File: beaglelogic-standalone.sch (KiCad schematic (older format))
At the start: 247 parts, among them J1 USB_OTG, J2 CONN_02X02, J3 USB_A, J4 CONN_01X06, J5 SI-51009-F, J6 CONN_02X12, J7 CONN_02X16, Q1 BSS138, Q2 BSS138, SW1 SW_PUSH_SMALL_H, SW2 SW_PUSH_SMALL_H, U1 74LVC1G07, U10 MCP79410/TDFN, U11 SST26VF064B, U12 TPS73101, U13 SN74LVCH16T245, U14 DVIULC6-4SC6, U15 DVIULC6-4SC6, U16 DVIULC6-4SC6, U17 DVIULC6-4SC6, U18 74LV1T125, U19 EMMC_4G, U2 AP1117, U3 TPS2051C, U4 TPD4S012, U5 TPD4S012, U6 OSD3358-SM, U7 KSZ9031RNXCC, U8 74LVC2G241, U9 74LVC1G125, Y1 25MHz, Y2 24MHz, Y3 32.768kHz,CL=9pF

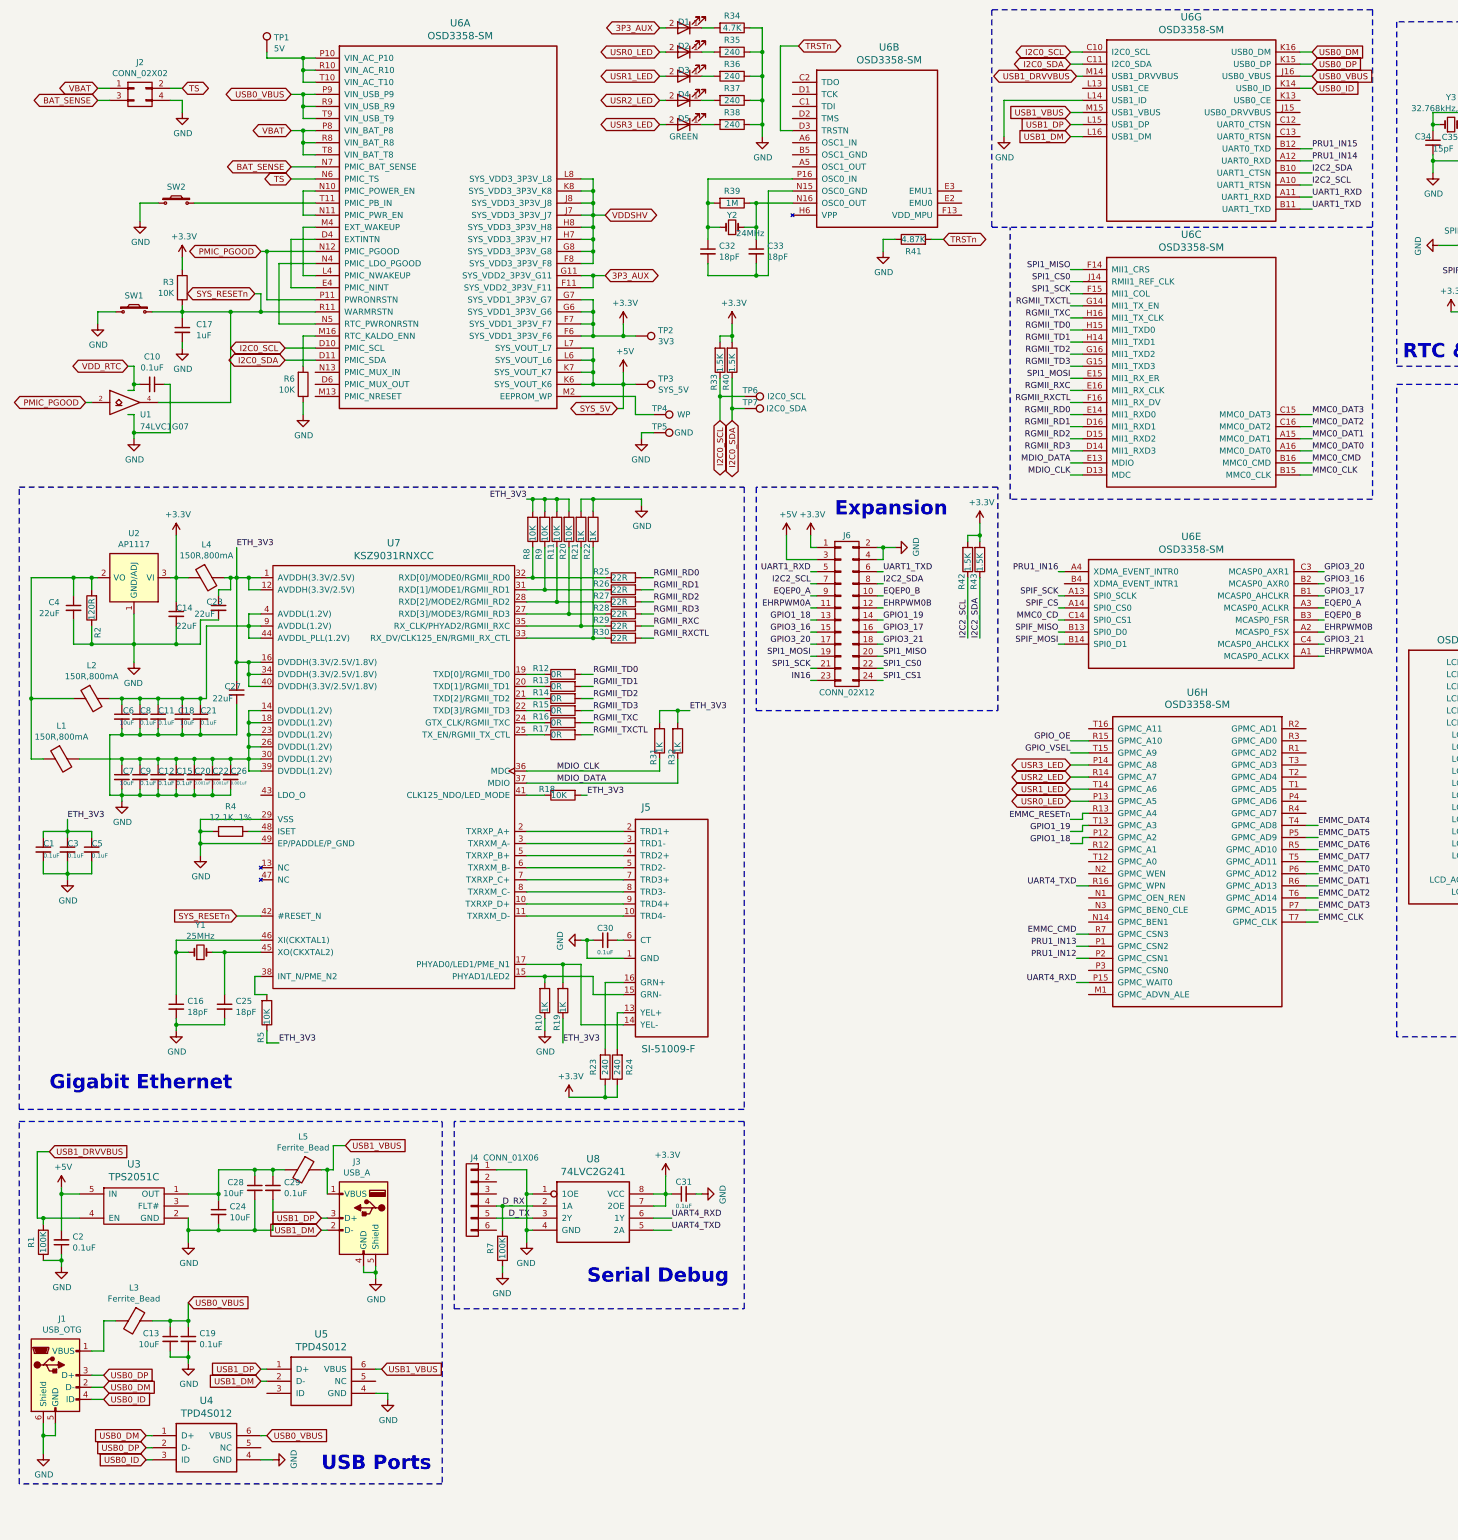
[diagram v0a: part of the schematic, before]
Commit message: PCB layout: Initial commit
First pass at component placement.
Also, slight changes in schematic.

Signed-off-by: Kumar Abhishek <abhishek@theembeddedkitchen.net>
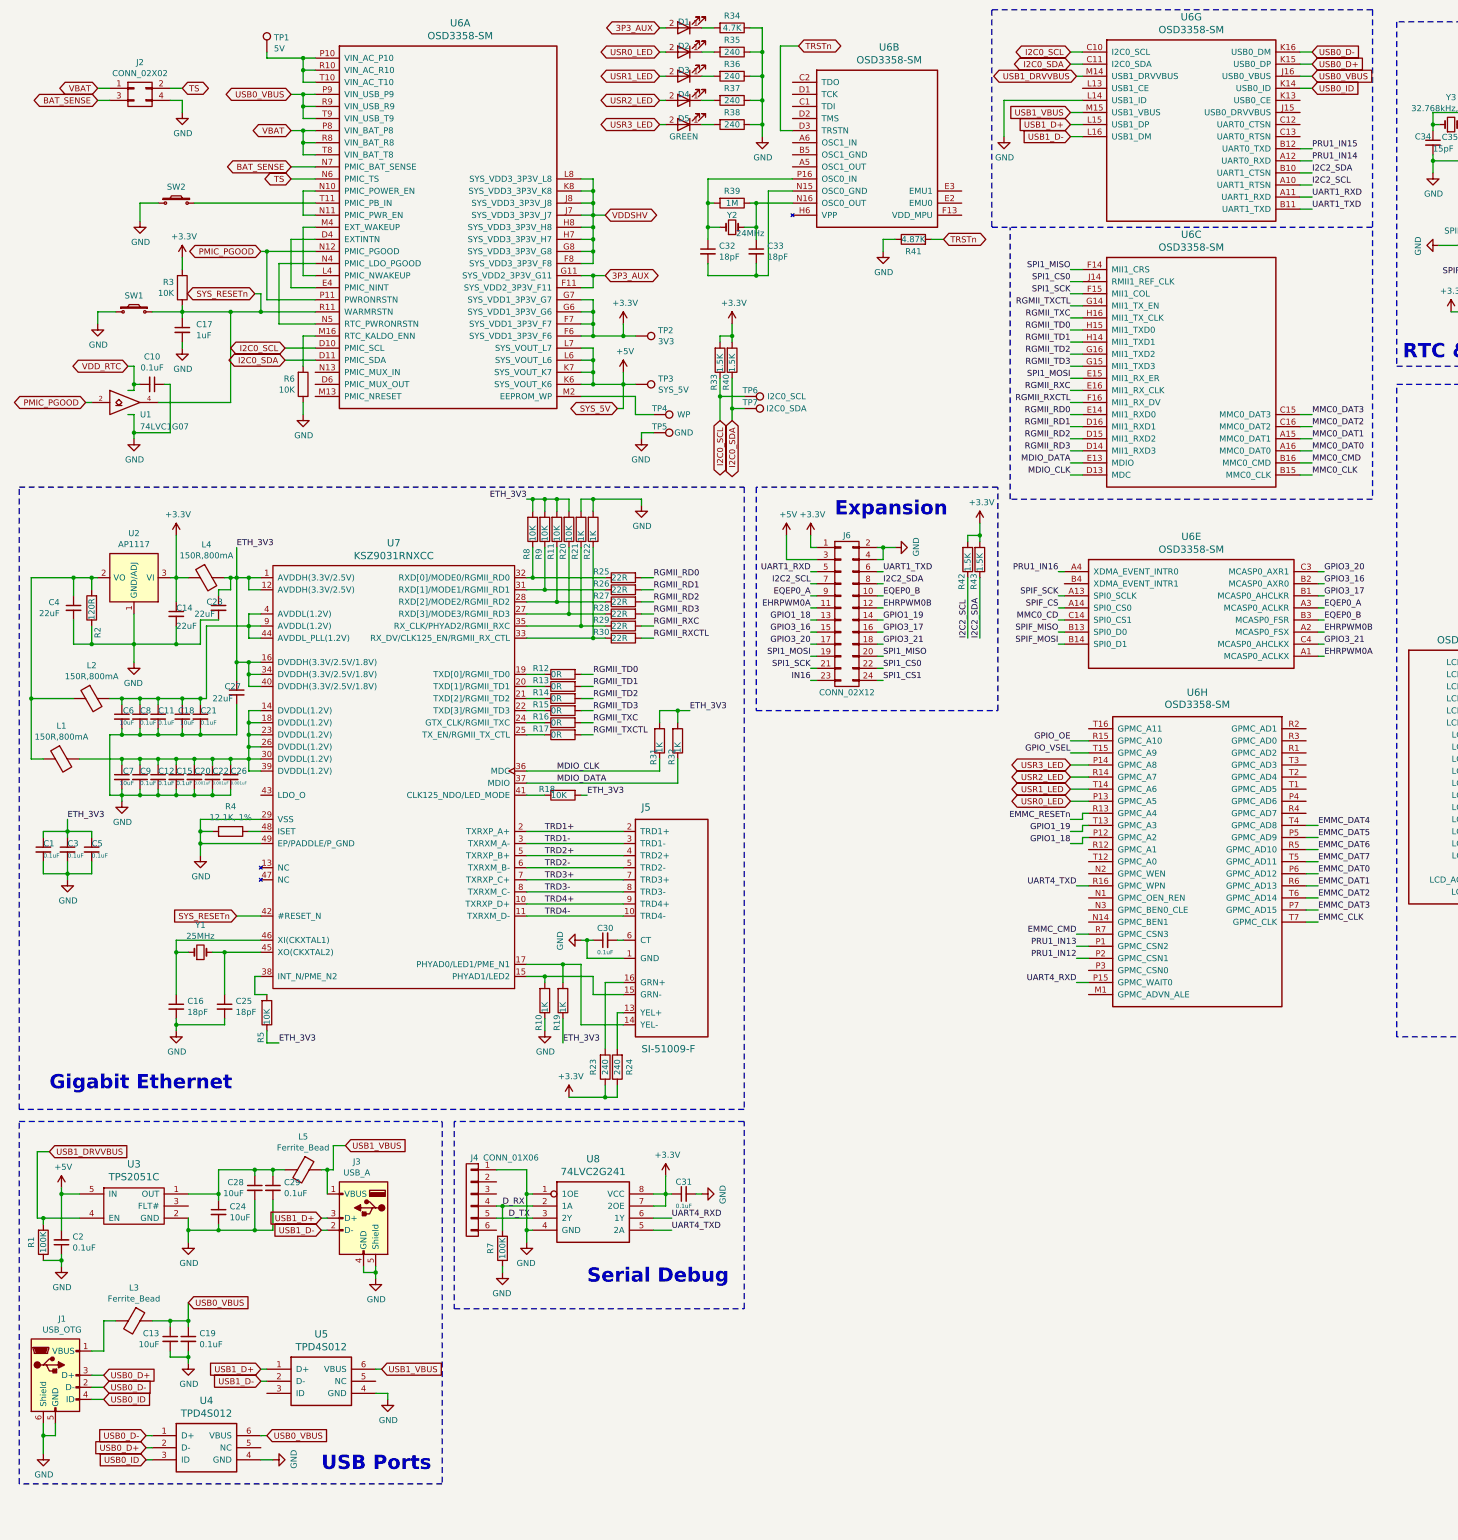
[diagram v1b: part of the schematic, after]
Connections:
- net TRD4-: now reaches J5.10 (TRD4-), U7.11 (TXRXM_D-)
- net TRD1+: now reaches J5.2 (TRD1+), U7.2 (TXRXP_A+)
- net TRD1-: now reaches J5.3 (TRD1-), U7.3 (TXRXM_A-)
- net TRD2+: now reaches J5.4 (TRD2+), U7.5 (TXRXP_B+)
- net TRD2-: now reaches J5.5 (TRD2-), U7.6 (TXRXM_B-)
- net TRD3+: now reaches J5.7 (TRD3+), U7.7 (TXRXP_C+)
- net TRD3-: now reaches J5.8 (TRD3-), U7.8 (TXRXM_C-)
- net TRD4+: now reaches J5.9 (TRD4+), U7.10 (TXRXP_D+)
- net USB0_DM renamed USB0_D-
- net USB0_DP renamed USB0_D+
- net USB1_DM renamed USB1_D-
- net USB1_DP renamed USB1_D+
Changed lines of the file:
@@
 MMC0_CD
 Text GLabel 1200 11900 2    50   Input ~ 0
-USB0_DM
+USB0_D-
 Text GLabel 1200 11800 2    50   Input ~ 0
-USB0_DP
+USB0_D+
 $Comp
 L Ferrite_Bead L3
@@
 $EndComp
 Text GLabel 3000 10500 0    50   Input ~ 0
-USB1_DP
+USB1_D+
 Text GLabel 3000 10600 0    50   Input ~ 0
-USB1_DM
+USB1_D-
 Text GLabel 3200 9900 2    50   Input ~ 0
 USB1_VBUS
@@
 USB1_VBUS
 Text GLabel 9200 1450 0    50   Input ~ 0
-USB1_DP
+USB1_D+
 Text GLabel 9200 1550 0    50   Input ~ 0
-USB1_DM
+USB1_D-
 $Comp
 L GND #PWR051
@@
 $EndComp
 Text GLabel 11200 850  2    50   Input ~ 0
-USB0_DM
+USB0_D-
 Text GLabel 11200 950  2    50   Input ~ 0
-USB0_DP
+USB0_D+
 Text GLabel 11200 1150 2    50   Input ~ 0
 USB0_ID
@@
 $EndComp
 Text GLabel 1550 12400 0    50   Input ~ 0
-USB0_DP
+USB0_D+
 Text GLabel 1550 12300 0    50   Input ~ 0
-USB0_DM
+USB0_D-
 Text GLabel 1550 12500 0    50   Input ~ 0
 USB0_ID
@@
 $EndComp
 Text GLabel 2500 11750 0    50   Input ~ 0
-USB1_DP
+USB1_D+
 Text GLabel 2500 11850 0    50   Input ~ 0
-USB1_DM
+USB1_D-
 $Comp
 L GND #PWR086
@@
 Connection ~ 17200 7400
 Connection ~ 18700 7400
+Text Label 4850 7300 0    50   ~ 0
+TRD1+
+Text Label 4850 7400 0    50   ~ 0
+TRD1-
+Text Label 4850 7500 0    50   ~ 0
+TRD2+
+Text Label 4850 7600 0    50   ~ 0
+TRD2-
+Text Label 4850 7700 0    50   ~ 0
+TRD3+
+Text Label 4850 7800 0    50   ~ 0
+TRD3-
+Text Label 4850 7900 0    50   ~ 0
+TRD4+
+Text Label 4850 8000 0    50   ~ 0
+TRD4-
 $EndSCHEMATC

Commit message: Update routing and schematic
Signed-off-by: Kumar Abhishek <abhishek@theembeddedkitchen.net>
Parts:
- removed TP1: 5V, Measurement_Points:Measurement_Point_Round-SMD-Pad_Small, symbol TEST_1P
- added J8: Barrel_Jack, Connect:BARREL_JACK, symbol Barrel_Jack
- added LOGO1: TEST_1P, beaglelogic-standalone:beaglelogic-logo, symbol Mounting_Hole
- added M1, M2, M3, M4: TEST_1P, Mounting_Holes:MountingHole_3.2mm_M3, symbol Mounting_Hole
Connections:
- net DIN00: now also U13.2 (1B1); no longer U13.23 (2B8)
- net DIN01: now also U13.3 (1B2); no longer U13.22 (2B7)
- net DIN02: now also U13.5 (1B3); no longer U13.20 (2B6)
- net DIN03: now also U13.6 (1B4); no longer U13.19 (2B5)
- net DIN04: now also U13.8 (1B5); no longer U13.17 (2B4)
- net DIN05: now also U13.9 (1B6); no longer U13.16 (2B3)
- net DIN06: now also U13.11 (1B7); no longer U13.14 (2B2)
- net DIN07: now also U13.12 (1B8); no longer U13.13 (2B1)
- net DIN08: now also U13.13 (2B1); no longer U13.12 (1B8)
- net DIN09: now also U13.14 (2B2); no longer U13.11 (1B7)
- net DIN10: now also U13.16 (2B3); no longer U13.9 (1B6)
- net DIN11: now also U13.17 (2B4); no longer U13.8 (1B5)
- net DIN12: now also U13.19 (2B5); no longer U13.6 (1B4)
- net DIN13: now also U13.20 (2B6); no longer U13.5 (1B3)
- net DIN14: now also U13.22 (2B7); no longer U13.3 (1B2)
- net DIN15: now also U13.23 (2B8); no longer U13.2 (1B1)
- net GND: now also J8.2
- net I2C2_SCL: now also J6.8 (P8); no longer J6.7 (P7)
- net I2C2_SDA: now also J6.7 (P7); no longer J6.8 (P8)
- net PRU1_IN00: now also U13.47 (1A1); no longer U13.26 (2A8)
- net PRU1_IN01: now also U13.46 (1A2); no longer U13.27 (2A7)
- net PRU1_IN02: now also U13.44 (1A3); no longer U13.29 (2A6)
- net PRU1_IN03: now also RN1.8 (R1.2), U13.43 (1A4); no longer RN1.5 (R4.2), U13.30 (2A5)
- net PRU1_IN04: now also RN1.7 (R2.2), U13.41 (1A5); no longer RN1.6 (R3.2), U13.32 (2A4)
- net PRU1_IN05: now also RN1.6 (R3.2), U13.40 (1A6); no longer RN1.7 (R2.2), U13.33 (2A3)
- net PRU1_IN06: now also U13.38 (1A7); no longer U13.35 (2A2)
- net PRU1_IN07: now also U13.37 (1A8); no longer U13.36 (2A1)
- net PRU1_IN08: now also U13.36 (2A1); no longer U13.37 (1A8)
- net PRU1_IN09: now also U13.35 (2A2); no longer U13.38 (1A7)
- net PRU1_IN10: now also U13.33 (2A3); no longer U13.40 (1A6)
- net PRU1_IN11: now also U13.32 (2A4); no longer U13.41 (1A5)
- net PRU1_IN12: now also U13.30 (2A5); no longer U13.43 (1A4)
- net PRU1_IN13: now also U13.29 (2A6); no longer U13.44 (1A3)
- net PRU1_IN14: now also U13.27 (2A7); no longer U13.46 (1A2)
- net PRU1_IN15: now also U13.26 (2A8); no longer U13.47 (1A1)
- net UART1_RXD: now also J6.6 (P6); no longer J6.5 (P5)
- net UART1_TXD: now also J6.5 (P5); no longer J6.6 (P6)
- net 5V_IN: now reaches U6.P10 (VIN_AC_P10), U6.R10 (VIN_AC_R10), U6.T10 (VIN_AC_T10)
- net 5V_IN: now also J8.1
- net at U6.L1 (LCD_DATA14): now also RN1.5 (R4.2); no longer RN1.8 (R1.2)
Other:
- note added: "Mounting holes\n"
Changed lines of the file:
@@
 LIBS:contrib
 LIBS:valves
+LIBS:mechanical
+LIBS:graphic_symbols
 LIBS:beaglelogic-standalone-cache
 EELAYER 26 0
@@
 L R_Pack04 RN1
 U 1 1 5961EA54
-P 13400 5550
-F 0 "RN1" H 13120 5504 50  0000 R CNN
-F 1 "100K" H 13120 5595 50  0000 R CNN
-F 2 "Resistors_SMD:R_Array_Concave_4x0402" V 13675 5550 50  0001 C CNN
-F 3 "" H 13400 5550 50  0001 C CNN
-	1    13400 5550
-	-1   0    0    1
+P 13500 5550
+F 0 "RN1" H 13220 5504 50  0000 R CNN
+F 1 "100K" H 13220 5595 50  0000 R CNN
+F 2 "Resistors_SMD:R_Array_Concave_4x0402" V 13775 5550 50  0001 C CNN
+F 3 "" H 13500 5550 50  0001 C CNN
+	1    13500 5550
+	1    0    0    1
 $EndComp
 $Comp
@@
 	1    0    0    -1
 $EndComp
-Text Label 17300 7900 0    50   ~ 0
+Text Label 17300 5800 0    50   ~ 0
 DIN00
-Text Label 17300 7800 0    50   ~ 0
+Text Label 17300 5900 0    50   ~ 0
 DIN01
 Text Label 21950 5650 2    50   ~ 0
@@
 Text Label 20200 5500 0    50   ~ 0
 IN02
-Text Label 17300 7600 0    50   ~ 0
+Text Label 17300 6100 0    50   ~ 0
 DIN02
-Text Label 17300 7500 0    50   ~ 0
+Text Label 17300 6200 0    50   ~ 0
 DIN03
-Text Label 17300 7300 0    50   ~ 0
+Text Label 17300 6400 0    50   ~ 0
 DIN04
-Text Label 17300 7200 0    50   ~ 0
+Text Label 17300 6500 0    50   ~ 0
 DIN05
-Text Label 17300 7000 0    50   ~ 0
+Text Label 17300 6700 0    50   ~ 0
 DIN06
-Text Label 17300 6900 0    50   ~ 0
-DIN07
 Text Label 17300 6800 0    50   ~ 0
+DIN07
+Text Label 17300 6900 0    50   ~ 0
 DIN08
-Text Label 17300 6700 0    50   ~ 0
+Text Label 17300 7000 0    50   ~ 0
 DIN09
-Text Label 17300 6500 0    50   ~ 0
+Text Label 17300 7200 0    50   ~ 0
 DIN10
-Text Label 17300 6400 0    50   ~ 0
+Text Label 17300 7300 0    50   ~ 0
 DIN11
-Text Label 17300 6200 0    50   ~ 0
+Text Label 17300 7500 0    50   ~ 0
 DIN12
-Text Label 17300 6100 0    50   ~ 0
+Text Label 17300 7600 0    50   ~ 0
 DIN13
-Text Label 17300 5900 0    50   ~ 0
+Text Label 17300 7800 0    50   ~ 0
 DIN14
-Text Label 17300 5800 0    50   ~ 0
+Text Label 17300 7900 0    50   ~ 0
 DIN15
 Text Label 19350 4950 2    50   ~ 0
@@
 	1    0    0    -1
 $EndComp
-Text Label 15200 7900 2    50   ~ 0
+Text Label 15200 5800 2    50   ~ 0
 PRU1_IN00
-Text Label 15200 7800 2    50   ~ 0
+Text Label 15200 5900 2    50   ~ 0
 PRU1_IN01
-Text Label 15200 7600 2    50   ~ 0
+Text Label 15200 6100 2    50   ~ 0
 PRU1_IN02
-Text Label 15200 7500 2    50   ~ 0
+Text Label 15200 6200 2    50   ~ 0
 PRU1_IN03
-Text Label 15200 7300 2    50   ~ 0
+Text Label 15200 6400 2    50   ~ 0
 PRU1_IN04
-Text Label 15200 7200 2    50   ~ 0
+Text Label 15200 6500 2    50   ~ 0
 PRU1_IN05
-Text Label 15200 7000 2    50   ~ 0
+Text Label 15200 6700 2    50   ~ 0
 PRU1_IN06
-Text Label 15200 6900 2    50   ~ 0
-PRU1_IN07
 Text Label 15200 6800 2    50   ~ 0
+PRU1_IN07
+Text Label 15200 6900 2    50   ~ 0
 PRU1_IN08
-Text Label 15200 6700 2    50   ~ 0
+Text Label 15200 7000 2    50   ~ 0
 PRU1_IN09
-Text Label 15200 6500 2    50   ~ 0
+Text Label 15200 7200 2    50   ~ 0
 PRU1_IN10
-Text Label 15200 6400 2    50   ~ 0
+Text Label 15200 7300 2    50   ~ 0
 PRU1_IN11
-Text Label 15200 6200 2    50   ~ 0
+Text Label 15200 7500 2    50   ~ 0
 PRU1_IN12
-Text Label 15200 6100 2    50   ~ 0
+Text Label 15200 7600 2    50   ~ 0
 PRU1_IN13
-Text Label 15200 5900 2    50   ~ 0
+Text Label 15200 7800 2    50   ~ 0
 PRU1_IN14
-Text Label 15200 5800 2    50   ~ 0
+Text Label 15200 7900 2    50   ~ 0
 PRU1_IN15
 $Comp
@@
 	1    0    0    -1
 $EndComp
-$Comp
-L TEST_1P TP1
-U 1 1 5976DB01
-P 2550 850
-F 0 "TP1" H 2608 970 50  0000 L CNN
-F 1 "5V" H 2608 879 50  0000 L CNN
-F 2 "Measurement_Points:Measurement_Point_Round-SMD-Pad_Small" H 2750 850 50  0001 C CNN
-F 3 "" H 2750 850 50  0001 C CNN
-	1    2550 850
-	1    0    0    -1
-$EndComp
 Text GLabel 1400 3450 0    50   BiDi ~ 0
 VDD_RTC
@@
 	-1   0    0    -1
 $EndComp
-Text Label 7050 5150 2    50   ~ 0
+Text Label 7650 5150 0    50   ~ 0
 UART1_RXD
 Text Label 11200 2050 0    50   ~ 0
@@
 Text Label 9250 7750 2    50   ~ 0
 UART4_TXD
-Text Label 7650 5150 0    50   ~ 0
+Text Label 7050 5150 2    50   ~ 0
 UART1_TXD
-Text Label 7650 5250 0    50   ~ 0
-I2C2_SDA
 Text Label 7050 5250 2    50   ~ 0
+I2C2_SDA
+Text Label 7650 5250 0    50   ~ 0
 I2C2_SCL
 Text Label 7050 5350 2    50   ~ 0
@@
 	2850 900  2850 1100
 Wire Wire Line
-	2550 900  2950 900
+	2750 900  2950 900
 Wire Wire Line
 	2950 1300 2850 1300
@@
 Wire Wire Line
 	1500 2100 1500 2250
-Wire Wire Line
-	2550 850  2550 900
 Connection ~ 2850 900
 Wire Wire Line
@@
 Wire Wire Line
 	16900 7400 18700 7400
-Connection ~ 17200 7400
-Connection ~ 18700 7400
 Text Label 4850 7300 0    50   ~ 0
 TRD1+
@@
 Text Label 4850 8000 0    50   ~ 0
 TRD4-
+Connection ~ 18700 7400
+Connection ~ 17200 7400
+$Comp
+L Mounting_Hole M1
+U 1 1 59A18719
+P 4550 11750
+F 0 "M1" H 4550 11895 50  0000 C CNN
+F 1 "TEST_1P" H 4608 11779 50  0001 L CNN
+F 2 "Mounting_Holes:MountingHole_3.2mm_M3" H 4750 11750 50  0001 C CNN
+F 3 "" H 4750 11750 50  0001 C CNN
+	1    4550 11750
+	1    0    0    -1
+$EndComp
+$Comp
+L Mounting_Hole M2
+U 1 1 59A1A3C5
+P 4750 11750
+F 0 "M2" H 4750 11895 50  0000 C CNN
+F 1 "TEST_1P" H 4808 11779 50  0001 L CNN
+F 2 "Mounting_Holes:MountingHole_3.2mm_M3" H 4950 11750 50  0001 C CNN
+F 3 "" H 4950 11750 50  0001 C CNN
+	1    4750 11750
+	1    0    0    -1
+$EndComp
+$Comp
+L Mounting_Hole M3
+U 1 1 59A1A5E5
+P 4950 11750
+F 0 "M3" H 4950 11895 50  0000 C CNN
+F 1 "TEST_1P" H 5008 11779 50  0001 L CNN
+F 2 "Mounting_Holes:MountingHole_3.2mm_M3" H 5150 11750 50  0001 C CNN
+F 3 "" H 5150 11750 50  0001 C CNN
+	1    4950 11750
+	1    0    0    -1
+$EndComp
+Wire Notes Line
+	4100 11300 4100 12700
+Wire Notes Line
+	4100 12700 6500 12700
+Wire Notes Line
+	6500 12700 6500 11300
+Wire Notes Line
+	6500 11300 4100 11300
+Text Notes 4950 12600 0    118  ~ 24
+Mounting holes\n
+$Comp
+L Mounting_Hole LOGO1
+U 1 1 59A1CFE2
+P 5500 11750
+F 0 "LOGO1" H 5600 11750 50  0000 L CNN
+F 1 "TEST_1P" H 5558 11779 50  0001 L CNN
+F 2 "beaglelogic-standalone:beaglelogic-logo" H 5700 11750 50  0001 C CNN
+F 3 "" H 5700 11750 50  0001 C CNN
+	1    5500 11750
+	1    0    0    -1
+$EndComp
+$Comp
+L Barrel_Jack J8
+U 1 1 59A1E8AF
+P 950 1700
+F 0 "J8" H 1028 2025 50  0000 C CNN
+F 1 "Barrel_Jack" H 1028 1934 50  0000 C CNN
+F 2 "Connect:BARREL_JACK" H 1000 1660 50  0001 C CNN
+F 3 "" H 1000 1660 50  0001 C CNN
+	1    950  1700
+	1    0    0    -1
+$EndComp
+$Comp
+L GND #PWR097
+U 1 1 59A224A3
+P 1350 1850
+F 0 "#PWR097" H 1350 1600 50  0001 C CNN
+F 1 "GND" H 1355 1677 50  0000 C CNN
+F 2 "" H 1350 1850 50  0001 C CNN
+F 3 "" H 1350 1850 50  0001 C CNN
+	1    1350 1850
+	1    0    0    -1
+$EndComp
+Wire Wire Line
+	1250 1800 1350 1800
+Wire Wire Line
+	1350 1800 1350 1850
+Text GLabel 2750 900  0    50   BiDi ~ 0
+5V_IN
+Text GLabel 1350 1600 2    50   BiDi ~ 0
+5V_IN
+Wire Wire Line
+	1350 1600 1250 1600
+$Comp
+L Mounting_Hole M4
+U 1 1 59A3557F
+P 5150 11750
+F 0 "M4" H 5150 11895 50  0000 C CNN
+F 1 "TEST_1P" H 5208 11779 50  0001 L CNN
+F 2 "Mounting_Holes:MountingHole_3.2mm_M3" H 5350 11750 50  0001 C CNN
+F 3 "" H 5350 11750 50  0001 C CNN
+	1    5150 11750
+	1    0    0    -1
+$EndComp
 $EndSCHEMATC

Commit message: Finalize board outline to 10cm x 6cm
Signed-off-by: Kumar Abhishek <abhishek@theembeddedkitchen.net>
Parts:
- J1: footprint Connect:USB_Micro-B -> beaglelogic-standalone:USB_MICRO_B_ST-USB-001E
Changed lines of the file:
@@
 F 0 "J1" H 855 12267 50  0000 C CNN
 F 1 "USB_OTG" H 855 12176 50  0000 C CNN
-F 2 "Connect:USB_Micro-B" H 950 11750 50  0001 C CNN
+F 2 "beaglelogic-standalone:USB_MICRO_B_ST-USB-001E" H 950 11750 50  0001 C CNN
 F 3 "" H 950 11750 50  0001 C CNN
 	1    800  11800
